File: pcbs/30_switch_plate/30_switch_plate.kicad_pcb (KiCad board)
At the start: 2 copper layers, 121.6 x 102.6 mm, 84 parts, among them SW1 SW_Push, SW10 SW_Push, SW11 SW_Push, SW12 SW_Push, SW13 SW_Push, SW14 SW_Push, SW15 SW_Push, SW16 SW_Push, SW17 SW_Push, SW18 SW_Push, SW19 SW_Push, SW2 SW_Push, SW20 SW_Push, SW21 SW_Push, SW22 SW_Push, SW23 SW_Push, SW24 SW_Push, SW25 SW_Push, SW26 SW_Push, SW27 SW_Push, SW28 SW_Push, SW29 SW_Push, SW3 SW_Push, SW30 SW_Push, SW4 SW_Push, SW5 SW_Push, SW6 SW_Push, SW7 SW_Push, SW8 SW_Push, SW9 SW_Push, U1 WS2812B, U10 WS2812B, U11 WS2812B, U12 WS2812B, U13 WS2812B, U14 WS2812B, U15 WS2812B, U16 WS2812B, U17 WS2812B, U18 WS2812B, U19 WS2812B, U2 WS2812B, U20 WS2812B, U21 WS2812B, U22 WS2812B, U3 WS2812B, U4 WS2812B, U5 WS2812B, U6 WS2812B, U7 WS2812B, U8 WS2812B, U9 WS2812B

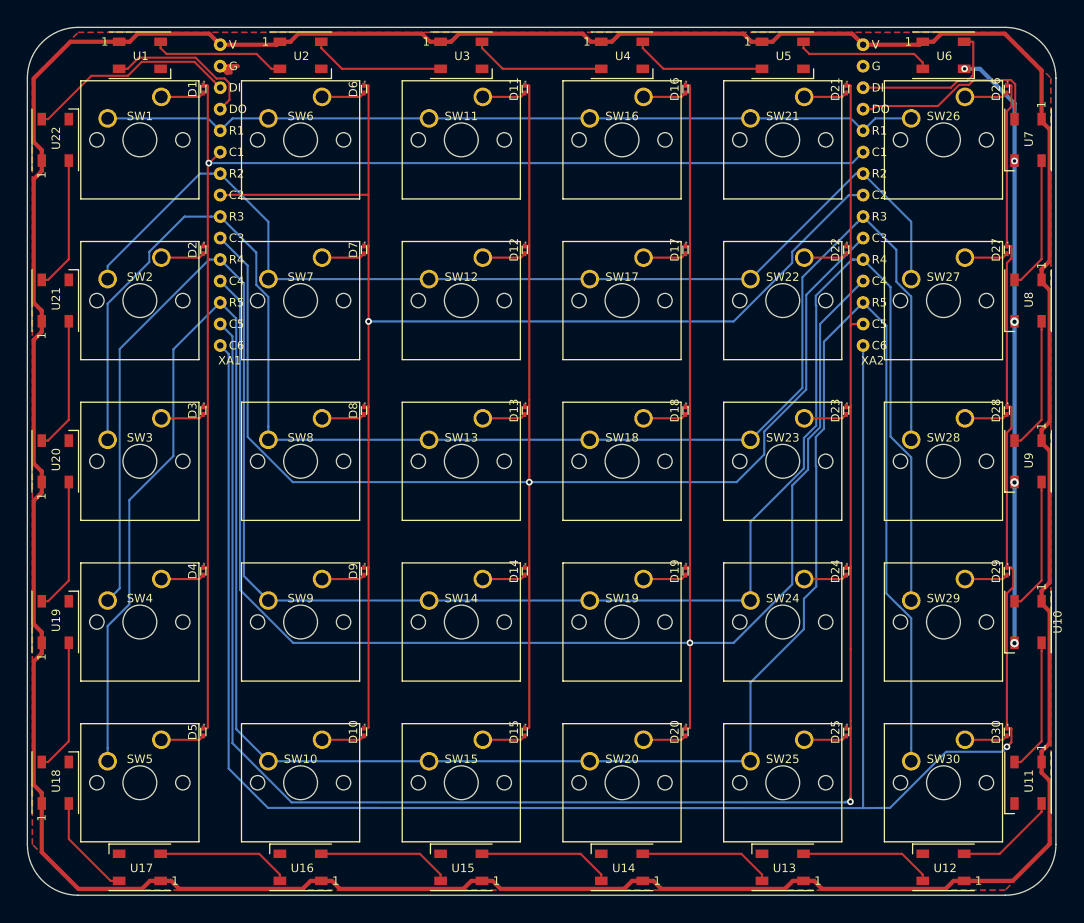
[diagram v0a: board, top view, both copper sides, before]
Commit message: Turn ws2812b orientation around
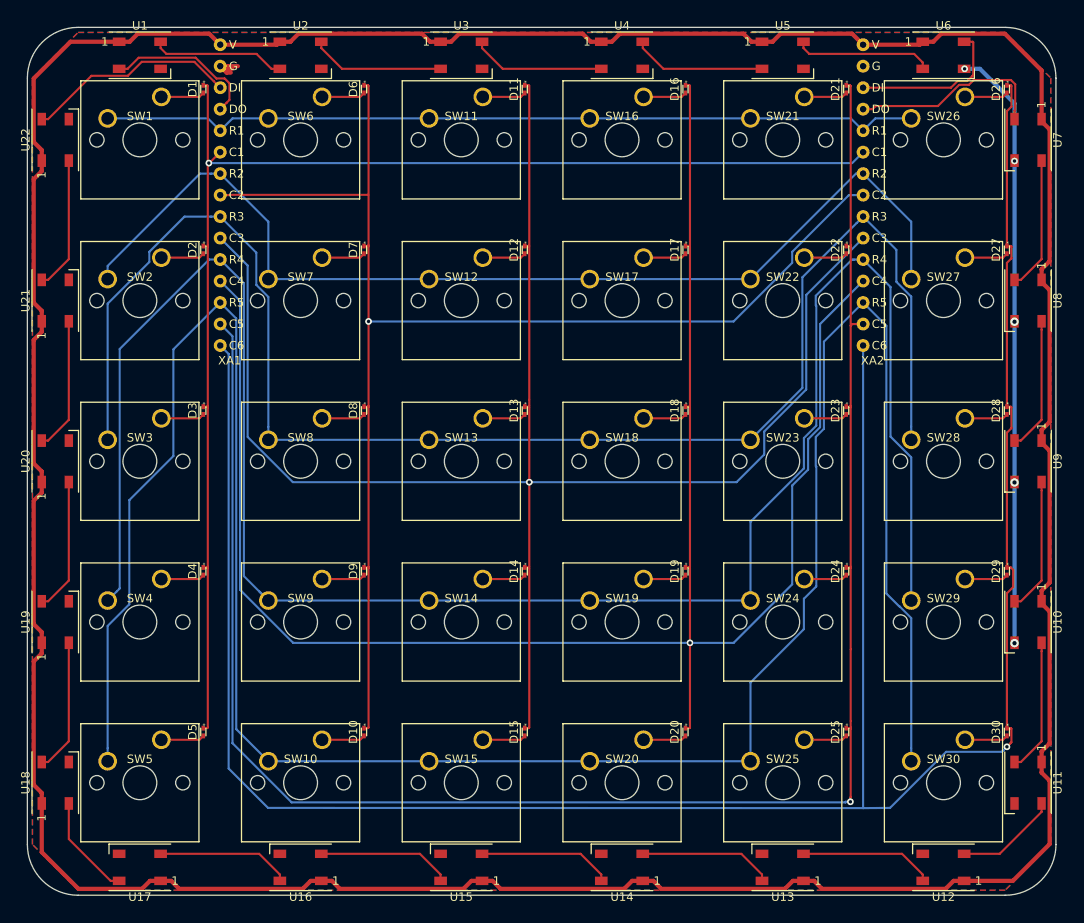
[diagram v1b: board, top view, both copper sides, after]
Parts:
- U1, U10, U11, U12, U13, U14, U15, U16, U17, U18, U19, U2, U20, U21, U22, U3, U4, U5, U6, U7, U8, U9: footprint LED_SMD:LED_WS2812B_PLCC4_5.0x5.0mm_P3.2mm -> footprints:LED_WS2812B_PLCC4_5.0x5.0mm_P3.2mm_WorldSemi
- turned U1 to 180 degrees
- turned U10 to 90 degrees
- turned U11 to 90 degrees
- turned U12 to 0 degrees
- turned U13 to 0 degrees
- turned U14 to 0 degrees
- turned U15 to 0 degrees
- turned U16 to 0 degrees
- turned U17 to 0 degrees
- turned U18 to 270 degrees
- turned U19 to 270 degrees
- turned U2 to 180 degrees
- turned U20 to 270 degrees
- turned U21 to 270 degrees
- turned U22 to 270 degrees
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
